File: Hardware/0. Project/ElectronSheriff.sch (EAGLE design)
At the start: 20 parts, among them Q2 AO3400, Q3 AO3400, U1 LM358D, U2 MAX4239AUTT

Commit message: Working on 1.0 schematic
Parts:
- U2: value MAX4239AUTT -> MAX4239
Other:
- moved on the sheet: C1
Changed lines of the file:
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@@
 <part name="R2" library="rcl" library_urn="urn:adsk.eagle:library:334" deviceset="R-EU_" device="R0603" package3d_urn="urn:adsk.eagle:package:23555/3" value="100k (1%)"/>
 <part name="BT1" library="1053" deviceset="1053" device="" value="CR2450"/>
-<part name="U2" library="MAX4239AUT+" deviceset="MAX4239AUTT" device=""/>
+<part name="U2" library="MAX4239AUT+" deviceset="MAX4239AUTT" device="" value="MAX4239"/>
 <part name="GND1" library="supply1" library_urn="urn:adsk.eagle:library:371" deviceset="0V" device=""/>
 <part name="PE1" library="supply1" library_urn="urn:adsk.eagle:library:371" deviceset="PE" device="" value=""/>
@@
 <attribute name="VALUE" x="242.57" y="73.66" size="1.778" layer="96" rot="R90"/>
 </instance>
-<instance part="C1" gate="G$1" x="254" y="113.03" smashed="yes">
-<attribute name="NAME" x="255.524" y="113.411" size="1.778" layer="95"/>
-<attribute name="VALUE" x="255.524" y="108.331" size="1.778" layer="96"/>
+<instance part="C1" gate="G$1" x="234.95" y="113.03" smashed="yes">
+<attribute name="NAME" x="236.474" y="113.411" size="1.778" layer="95"/>
+<attribute name="VALUE" x="236.474" y="108.331" size="1.778" layer="96"/>
 </instance>
 <instance part="R7" gate="G$1" x="199.39" y="130.81" smashed="yes">
@@
 <attribute name="VALUE" x="128.27" y="118.618" size="1.6764" layer="96"/>
 </instance>
-<instance part="PE5" gate="M" x="125.73" y="90.17" smashed="yes">
-<attribute name="VALUE" x="123.19" y="87.63" size="1.778" layer="96" rot="R90"/>
+<instance part="PE5" gate="M" x="125.73" y="76.2" smashed="yes">
+<attribute name="VALUE" x="123.19" y="73.66" size="1.778" layer="96" rot="R90"/>
 </instance>
 <instance part="R9" gate="G$1" x="153.67" y="120.65" smashed="yes" rot="R90">
@@
 <segment>
 <pinref part="PE5" gate="M" pin="PE"/>
-<wire x1="125.73" y1="92.71" x2="125.73" y2="95.25" width="0.1524" layer="91"/>
+<wire x1="125.73" y1="78.74" x2="125.73" y2="95.25" width="0.1524" layer="91"/>
 <pinref part="X1" gate="-2" pin="KL"/>
 <wire x1="113.03" y1="95.25" x2="125.73" y2="95.25" width="0.1524" layer="91"/>
@@
 <pinref part="U2" gate="A" pin="OUT"/>
 <pinref part="R4" gate="G$1" pin="2"/>
-<wire x1="227.33" y1="128.27" x2="245.11" y2="128.27" width="0.1524" layer="91"/>
+<wire x1="227.33" y1="128.27" x2="234.95" y2="128.27" width="0.1524" layer="91"/>
+<wire x1="234.95" y1="128.27" x2="245.11" y2="128.27" width="0.1524" layer="91"/>
 <wire x1="245.11" y1="128.27" x2="245.11" y2="124.46" width="0.1524" layer="91"/>
 <pinref part="C1" gate="G$1" pin="1"/>
-<wire x1="254" y1="115.57" x2="254" y2="128.27" width="0.1524" layer="91"/>
-<wire x1="254" y1="128.27" x2="245.11" y2="128.27" width="0.1524" layer="91"/>
-<junction x="245.11" y="128.27"/>
+<wire x1="234.95" y1="115.57" x2="234.95" y2="128.27" width="0.1524" layer="91"/>
+<junction x="234.95" y="128.27"/>
 </segment>
 </net>
@@
 <wire x1="209.55" y1="125.73" x2="207.01" y2="125.73" width="0.1524" layer="91"/>
 <wire x1="207.01" y1="125.73" x2="207.01" y2="95.25" width="0.1524" layer="91"/>
-<wire x1="207.01" y1="95.25" x2="245.11" y2="95.25" width="0.1524" layer="91"/>
+<wire x1="207.01" y1="95.25" x2="234.95" y2="95.25" width="0.1524" layer="91"/>
 <pinref part="R5" gate="G$1" pin="1"/>
+<wire x1="234.95" y1="95.25" x2="245.11" y2="95.25" width="0.1524" layer="91"/>
 <wire x1="245.11" y1="95.25" x2="245.11" y2="99.06" width="0.1524" layer="91"/>
 <pinref part="R6" gate="G$1" pin="2"/>
@@
 <junction x="245.11" y="95.25"/>
 <pinref part="C1" gate="G$1" pin="2"/>
-<wire x1="254" y1="107.95" x2="254" y2="95.25" width="0.1524" layer="91"/>
-<wire x1="254" y1="95.25" x2="245.11" y2="95.25" width="0.1524" layer="91"/>
-</segment>
-</net>
+<wire x1="234.95" y1="107.95" x2="234.95" y2="95.25" width="0.1524" layer="91"/>
+<junction x="234.95" y="95.25"/>
+</segment>
+</net>

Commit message: Working on 1.0 schematic
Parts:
- added C10, C13: 15 pF, rcl:C-EUC0603
- added C11, C5: DNP, rcl:C-EUC0603
- added C12, C9: 6 pF, rcl:C-EUC0603
- added C14: 0.8 pF, rcl:C-EUC0603
- added C18, C19, C7, C8: 100 nF, rcl:C-EUC0603
- added C20, C22: 1uF, rcl:C-EUC0603
- added C21: 4.7 uF, rcl:C-EUC0603
- added C6: 100 pF, rcl:C-EUC0603
- added E1: ANT, SparkFun-RF:ANTENNA-GROUNDEDTRACE-15.2MM
- added J1: (no value), SparkFun-Connectors:ARDUINO_SERIAL_PROGRAMPTH
- added J5: CORTEX_DEBUGPTH, SparkFun-Connectors:CORTEX_DEBUGPTH
- added JP1: VDD-EN, SparkFun-Jumpers:JUMPER-SMT_2_NC_TRACE_SILK
- added L1: 3.9nH, nrf52832-breakout-temp:INDUCTOR-0402-3.9NH
- added SW1: TACTILE_SWITCH_SMD_4_6X2_8MM, SparkFun-Electromechanical:SWITCH_SPST_4_PINRECT
- added TP1, TP2: TEST-POINT3X4, SparkFun-Connectors:TEST-POINT3X4
- added U3: NRF52832, nrf52832-breakout-temp:NRF52832
- added U5: LM321MF, linear:LM321MF
- added Y1: 32MHz, nrf52832-breakout-temp:CRYSTAL-32MHZ-SMD-2.0X1.6MM
- added Y2: 32.768kHz, SparkFun-Clocks:CRYSTAL-32.768KHZSMD-3.2X1.5
- U1: value LM358D -> XC6206; device linear:LM358D -> XC6206:PMIC-LDO-XC6206P332MR-G(SOT23)
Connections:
- new net BLE_ANT: C14.1, L1.2, U3.ANT
- new net CRYSTAL_XC1: C12.1, U3.XC1(32MHZ), Y1.2
- new net CRYSTAL_XC2: C9.1, U3.XC2(32MHZ), Y1.1
- new net CRYSTAL_XL1: C10.1, U3.P0.00/XL1, Y2.2
- new net CRYSTAL_XL2: C13.1, U3.P0.01/XL2, Y2.1
- new net GND: C20.2, C22.2, J1.GND, J5.GND@3, J5.GND@5, J5.GNDDTCT, SW1.3, SW1.4, U1.GND
- new net MCU_!RESET!: J5.!RESET, SW1.1, SW1.2, U3.P0.21/RESET
- new net N$11: C11.1, E1.SIGNAL, L1.1
- new net N$12: C5.1, U3.DEC2
- new net N$13: C6.1, U3.DEC3
- new net N$14: J1.VCC, JP1.1
- new net N$15: C7.1, U3.DEC4
- new net N$8: C18.1, U3.DEC1
- new net P02: U3.P0.02/AIN0
- new net P03: U3.P0.03/AIN1
- new net P04: U3.P0.04/AIN2
- new net P05: U3.P0.05/AIN3
- new net P06: U3.P0.06
- new net P07: U3.P0.07
- new net P08: U3.P0.08
- new net P11: U3.P0.11
- new net P12: U3.P0.12
- new net P13: U3.P0.13
- new net P14: U3.P0.14
- new net P15: U3.P0.15
- new net P16: U3.P0.16
- new net P17: U3.P0.17
- new net P18: J5.SWO/TDO, U3.P0.18
- new net P19: U3.P0.19
- new net P20: U3.P0.20
- new net P22: U3.P0.22
- new net P23: U3.P0.23
- new net P24: U3.P0.24
- new net P25: U3.P0.25
- new net P26: J1.TXO, U3.P0.26
- new net P27: J1.RXI, U3.P0.27
- new net P28: U3.P0.28/AIN4
- new net P29: U3.P0.29/AIN5
- new net P30: U3.P0.30/AIN6
- new net P31: U3.P0.31/AIN7
- new net SWDCLK: J5.SWDCLK/TCK, TP2.1, U3.SWDCLK
- new net SWDIO: J5.SWDIO/TMS, TP1.1, U3.SWDIO
- new net VDD: C19.1, C20.1, C21.1, C8.1, J5.VCC, JP1.2, U1.OUT, U3.VDD
- new net VIN: C22.1, U1.IN
- net +5V: now also U5.V+; no longer U1P.V+
- net 0V: now also C10.2, C11.2, C12.2, C13.2, C14.2, C18.2, C19.2, C21.2, C5.2, C6.2, C7.2, C8.2, C9.2, E1.GND, U3.VSS, U5.V-; no longer U1P.V-
- net N$2: now also U5.+IN; no longer U1A.+IN
- net N$4: now also U5.-IN, U5.OUT; no longer U1A.-IN, U1A.OUT
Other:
- note added: "Buttons"
- note added: "Cortex Debug Connector"
- note added: "Open JP1 to disable powering the nRF52832 via a 3.3V FTDI Basic"
- note added: "Pin 13"
- note added: "Pin 36"
- note added: "Pin 48"
- note added: "Serial Program/Debug"

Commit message: Working on 1.0 schematic
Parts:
- removed SW1: TACTILE_SWITCH_SMD_4_6X2_8MM, SparkFun-Electromechanical:SWITCH_SPST_4_PINRECT
- removed TP1, TP2: TEST-POINT3X4, SparkFun-Connectors:TEST-POINT3X4
- removed U1: XC6206, XC6206:PMIC-LDO-XC6206P332MR-G(SOT23)
- added C15: 100 nF, rcl:C-EUC0603
- added C16: 1uF, rcl:C-EUC0603
- added C17: 100nF, rcl:C-EUC0603
- added S1: DTSM-3, switch-tact:DTSM-3
- C20: value 1uF -> 100nF
- C22: value 1uF -> 10uF; device rcl:C-EUC0603 -> rcl:C-EUC0805
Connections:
- net N$1 renamed ADC_AMMETER
- net P18 renamed MCU_SWO/TDO
- removed net GND: C20.2, C22.2, J1.GND, J5.GND@3, J5.GND@5, J5.GNDDTCT, SW1.3, SW1.4, U1.GND
- removed net MCU_!RESET!: J5.!RESET, SW1.1, SW1.2, U3.P0.21/RESET
- removed net SWDCLK: J5.SWDCLK/TCK, TP2.1, U3.SWDCLK
- removed net SWDIO: J5.SWDIO/TMS, TP1.1, U3.SWDIO
- removed net VIN: C22.1, U1.IN
- new net !MCU_RESET!: J5.!RESET, S1.2, U3.P0.21/RESET
- new net MCU_SWDCLK/TCK: J5.SWDCLK/TCK, U3.SWDCLK
- new net MCU_SWDIO/TMS: J5.SWDIO/TMS, U3.SWDIO
- new net MCU_TDI: J5.NC/TDI
- net +5V: now also C15.1, C16.1, C17.1, C19.1, C21.1, C8.1, J5.VCC, U3.VDD
- net 0V: now also C15.2, C16.2, C17.2, C20.2, C22.2, J1.GND, J5.GND@3, J5.GND@5, J5.GNDDTCT, S1.1
- net N$2: now also C20.1, C22.1
- net VDD: no longer C19.1, C20.1, C21.1, C8.1, J5.VCC, U1.OUT, U3.VDD
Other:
- note added: "2.4 GHz Bluetooth Transceiver"
- note added: "Bootloader Program and Debug Interface"
- note added: "JTAG/SWD Program and Debug Interface"
- note added: "Load Current Sense and Signal Conditioning"
- note added: "MCU External Oscillators"
- note added: "MCU Reset"
- note added: "Power Supply"
- note added: "Virtual Ground Reference"
- note added: "nRF52 SoC (Cortex M4 + Bluetooth 5)"
- note removed: "Buttons"
- note removed: "Cortex Debug Connector"
- note removed: "Serial Program/Debug"
- moved on the sheet: BT1, C1, C10, C11, C12, C13, C14, C18, C19, C2, C20, C21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

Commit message: Working on 1.0 schematic
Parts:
- removed C4: 100nF, rcl:C-EUC0603
- added R11: 220R (5%), rcl:R-EU_R0603
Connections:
- net 0V: now also C3.2; no longer C4.1
- net ADC_AMMETER: now also R11.1, R11.2
- net PE: no longer C3.2, C4.2
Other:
- moved on the sheet: BT1, C1, C10, C11, C12, C13, C14, C15, C16, C17, C18, C19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

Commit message: Working on 1.0 schematic
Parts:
- removed JP1: VDD-EN, SparkFun-Jumpers:JUMPER-SMT_2_NC_TRACE_SILK
- added C23, C4: 100nF, rcl:C-EUC0603
- added CN1: MicroSD Card, Micro SD:MICROSD-PUSH-OUT
- added CN2: DISPLAY-OLED-128X64-I2C, diy-modules:DISPLAY-OLED-128X64-I2C
- added R12: 0R (5%), rcl:R-EU_R0603
- added R13, R14, R15, R16, R17: 10k (5%), rcl:R-EU_R0603
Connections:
- removed net N$14: J1.VCC, JP1.1
- removed net PE: Q2.S, Q3.S, R3.2, R6.1, R8.1, X1-2.KL
- removed net VDD: JP1.2
- new net !MICROSD_SPI_CS!: CN1.2
- new net ADC_AMMETER_VOUT: R11.2
- new net ADC_VGND: R12.2
- new net DISPLAY_I2C_SCL: CN2.SCL, R16.1
- new net DISPLAY_I2C_SDA: CN2.SDA, R17.1
- new net MICROSD_SPI_CARD_DETECT: CN1.9, R15.1
- new net MICROSD_SPI_CLK: CN1.5
- new net MICROSD_SPI_MISO: CN1.7, R14.1
- new net MICROSD_SPI_MOSI: CN1.3, R13.1
- new net RANGE_MA: Q3.G
- new net RANGE_UA: Q2.G
- new net VGND: Q2.S, Q3.S, R12.1, R3.2, R6.1, R8.1, X1-2.KL
- net +5V: now also C23.1, C4.1, CN1.4, CN2.VCC, R13.2, R14.2, R15.2, R16.2, R17.2
- net 0V: now also C23.2, C4.2, CN1.10, CN1.6, CN2.GND
- net ADC_AMMETER: no longer R11.2
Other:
- note added: "Micro SD Memory Card interface"
- note removed: "Open JP1 to disable powering the nRF52832 via a 3.3V FTDI Basic"
- moved on the sheet: BT1, C1, C10, C11, C12, C13, C14, C15, C16, C17, C18, C19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

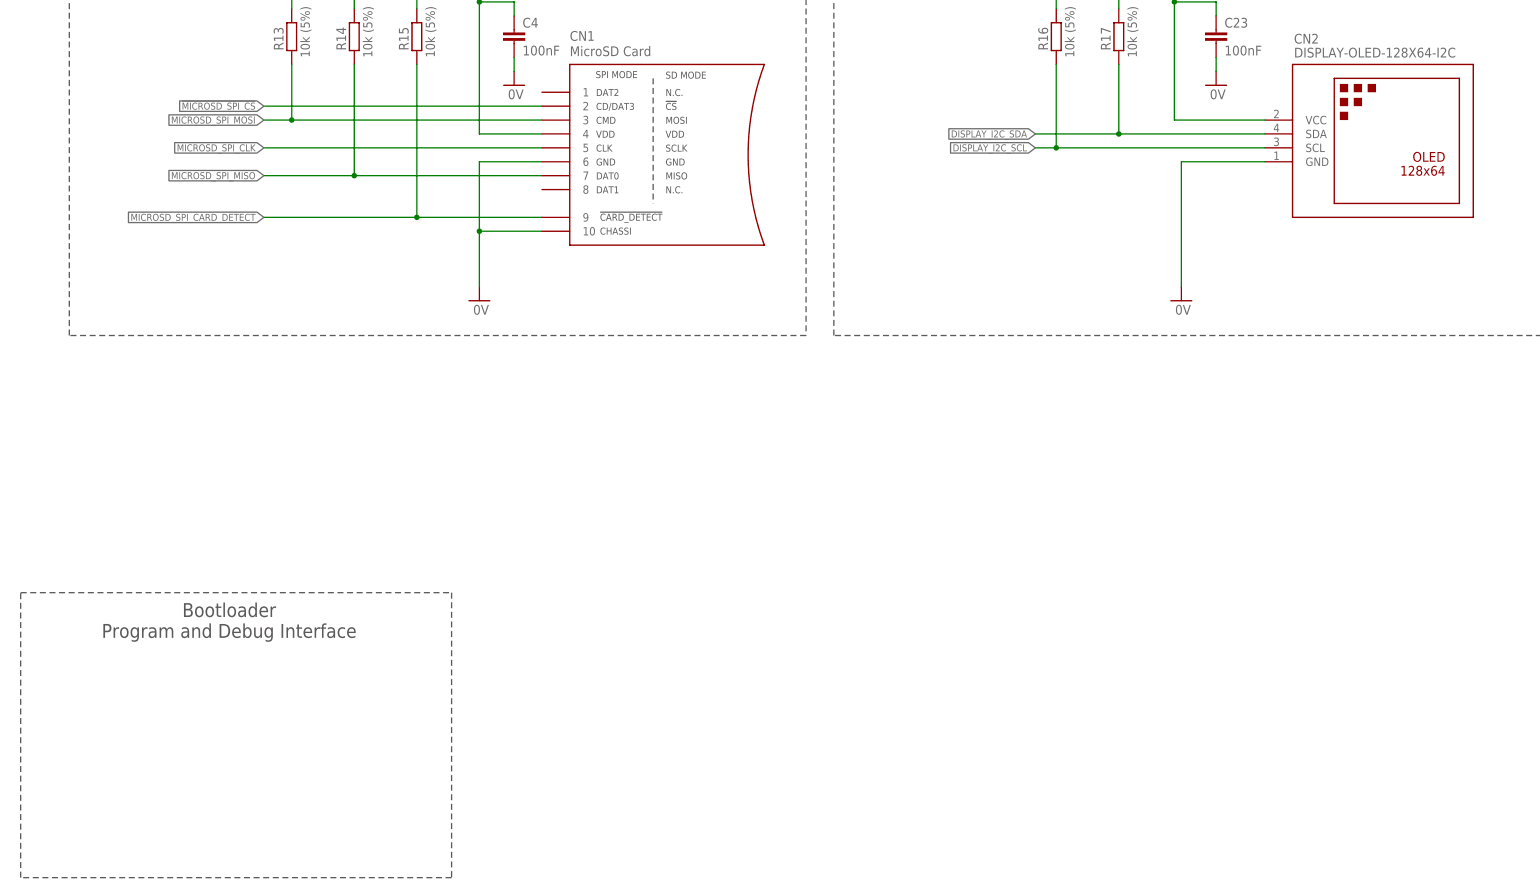
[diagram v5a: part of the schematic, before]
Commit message: OLED and SD-Card circuits added
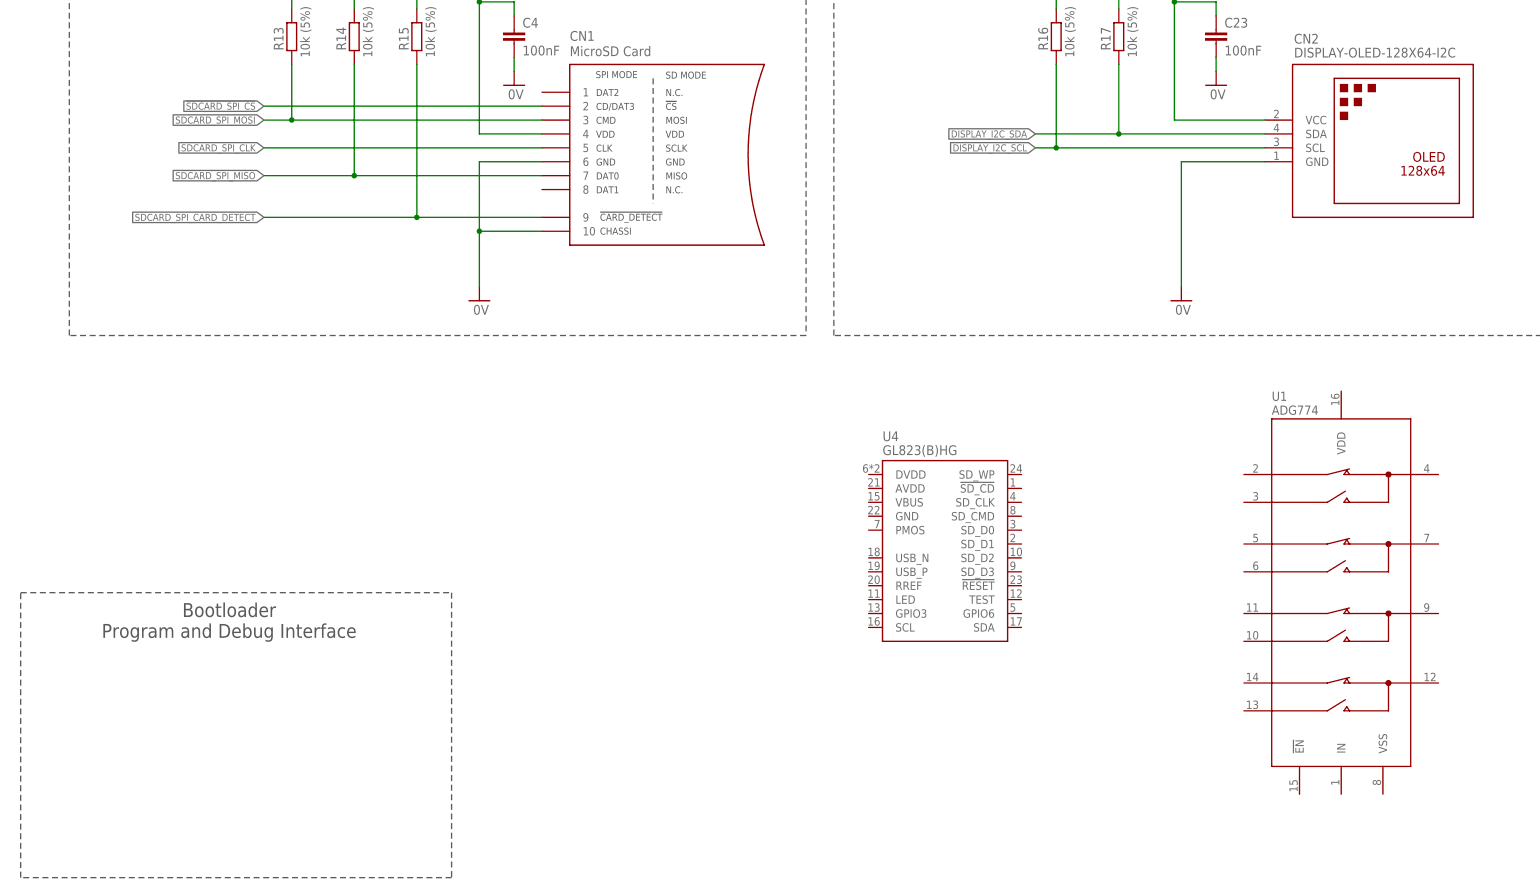
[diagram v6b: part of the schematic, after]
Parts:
- added U1: ADG774, ADG774:ADG774
- added U4: GL823(B)HG, GL823:GL823(B)HG
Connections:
- net !MICROSD_SPI_CS! renamed !SDCARD_SPI_CS!
- net MICROSD_SPI_CARD_DETECT renamed SDCARD_SPI_CARD_DETECT
- net MICROSD_SPI_CLK renamed SDCARD_SPI_CLK
- net MICROSD_SPI_MISO renamed SDCARD_SPI_MISO
- net MICROSD_SPI_MOSI renamed SDCARD_SPI_MOSI
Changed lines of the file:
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@@
 <setting verticaltext="up"/>
 </settings>
-<grid distance="0.05" unitdist="inch" unit="inch" style="lines" multiple="1" display="no" altdistance="0.01" altunitdist="inch" altunit="inch"/>
+<grid distance="0.1" unitdist="inch" unit="inch" style="lines" multiple="1" display="no" altdistance="0.01" altunitdist="inch" altunit="inch"/>
 <layers>
 <layer number="1" name="Top" color="4" fill="1" visible="no" active="no"/>
@@
 <part name="GND31" library="supply1" library_urn="urn:adsk.eagle:library:371" deviceset="0V" device=""/>
 <part name="GND32" library="supply1" library_urn="urn:adsk.eagle:library:371" deviceset="0V" device=""/>
+<part name="U4" library="GL823" deviceset="GL823(B)" device="HG"/>
+<part name="U1" library="ADG774" deviceset="ADG774" device=""/>
 </parts>
 <sheets>
@@
 <attribute name="VALUE" x="627.507" y="161.29" size="1.778" layer="96"/>
 </instance>
+<instance part="U4" gate="G$1" x="584.2" y="119.38" smashed="yes">
+<attribute name="NAME" x="574.04" y="138.176" size="1.778" layer="95"/>
+<attribute name="VALUE" x="574.04" y="135.636" size="1.778" layer="96"/>
+</instance>
+<instance part="U1" gate="G$1" x="655.32" y="109.22" smashed="yes">
+<attribute name="NAME" x="645.16" y="145.542" size="1.6764" layer="95"/>
+<attribute name="VALUE" x="645.16" y="143.002" size="1.6764" layer="95"/>
+</instance>
 </instances>
 <busses>
@@
 </segment>
 </net>
-<net name="!MICROSD_SPI_CS!" class="0">
+<net name="!SDCARD_SPI_CS!" class="0">
 <segment>
 <pinref part="CN1" gate="G$1" pin="2"/>
@@
 </segment>
 </net>
-<net name="MICROSD_SPI_MOSI" class="0">
+<net name="SDCARD_SPI_MOSI" class="0">
 <segment>
 <pinref part="CN1" gate="G$1" pin="3"/>
@@
 </segment>
 </net>
-<net name="MICROSD_SPI_CLK" class="0">
+<net name="SDCARD_SPI_CLK" class="0">
 <segment>
 <pinref part="CN1" gate="G$1" pin="5"/>
@@
 </segment>
 </net>
-<net name="MICROSD_SPI_MISO" class="0">
+<net name="SDCARD_SPI_MISO" class="0">
 <segment>
 <pinref part="CN1" gate="G$1" pin="7"/>
@@
 </segment>
 </net>
-<net name="MICROSD_SPI_CARD_DETECT" class="0">
+<net name="SDCARD_SPI_CARD_DETECT" class="0">
 <segment>
 <pinref part="CN1" gate="G$1" pin="9"/>

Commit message: SD-Card to USB Circuit Interface Added
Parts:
- added C24, C25, C27, C28, C29: 100nF, rcl:C-EUC0603
- added C26: 10uF, rcl:C-EUC0603
- added L3: BLM15HB221SN1, inductors:BLM15HB221SN1
- added LED1: (no value), led:LEDCHIPLED_0603
- added Q1: BC817, transistor-npn:BC817-16LT1SMD
- added R18, R20, R21: 10k (5%), rcl:R-EU_R0603
- added R19: 4K7 (5%), rcl:R-EU_R0603
- added R22: 680R (5%), rcl:R-EU_R0603
- added R23: 1k (5%), rcl:R-EU_R0603
- added U6: ADG774, ADG774:ADG774
- added X2: (no value), con-berg:PN87520
- U4: value GL823(B)HG -> GL823
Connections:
- removed net !SDCARD_SPI_CS!: CN1.2
- removed net SDCARD_SPI_CARD_DETECT: CN1.9, R15.1
- removed net SDCARD_SPI_CLK: CN1.5
- removed net SDCARD_SPI_MISO: CN1.7, R14.1
- removed net SDCARD_SPI_MOSI: CN1.3, R13.1
- new net !MCU_SPI_CS!: U1.S4B
- new net MCU_SPI_CLK: U6.S2B
- new net MCU_SPI_MISO: U1.S1B
- new net MCU_SPI_MOSI: U6.S1B
- new net MUX_SWITCH: Q1.C, R18.1, R21.1, U1.IN, U6.IN
- new net N$1: C26.2, C27.2, L3.1, U4.DVDD
- new net N$14: Q1.B, R19.1
- new net N$16: C28.2, U4.PMOS
- new net N$17: C29.2, U4.!RESET
- new net N$18: R22.1, U4.RREF
- new net N$19: L3.2, U4.AVDD
- new net N$21: U4.USB_N, X2.2
- new net N$22: U4.USB_P, X2.3
- new net N$23: R23.1, U4.LED
- new net N$24: LED1.A, R23.2
- new net SDCARD_CARD_DETECT: CN1.9, R15.1, U4.!SD_CD
- new net SDCARD_CLK: CN1.5, U6.D2
- new net SDCARD_CMD/MOSI: CN1.3, R13.1, U6.D1
- new net SDCARD_DAT0/MISO: CN1.7, R14.1, U1.D1
- new net SDCARD_DAT1: CN1.8, U1.D2
- new net SDCARD_DAT2: CN1.1, U1.D3
- new net SDCARD_DAT3/!CS!: CN1.2, U1.D4
- new net USB_CLK: U4.SD_CLK, U6.S2A
- new net USB_CMD: U4.SD_CMD, U6.S1A
- new net USB_DAT0: U1.S1A, U4.SD_D0
- new net USB_DAT1: U1.S2A, U4.SD_D1
- new net USB_DAT2: U1.S3A, U4.SD_D2
- new net USB_DAT3: U1.S4A, U4.SD_D3
- new net USB_VDD: R19.2, R20.1, U4.VBUS, X2.1
- net +5V: now also C24.1, C25.1, R18.2, R21.2, U1.VDD, U6.VDD
- net 0V: now also C24.2, C25.2, C26.1, C27.1, C28.1, C29.1, LED1.C, Q1.E, R20.2, R22.2, U1.!EN!, U1.VSS, U4.GND, U4.GPIO3, U4.GPIO6, U4.SCL, U4.SDA, U4.SD_WP, U4.TEST, U6.!EN!, U6.VSS, X2.4
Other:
- note added: "Micro SD-Card to USB Interface"
- moved on the sheet: CN1, CN2, R16, R17, U4

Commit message: Working on 1.0 schematic
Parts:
- removed R11: 220R (5%), rcl:R-EU_R0603
- added C30, C31, C32: 100nF, rcl:C-EUC0603
- added R24: 68k (0.05%), rcl:R-EU_R0603
- added R25: 10k (0.05%), rcl:R-EU_R0603
- added R26: 220R (5%), rcl:R-EU_R0603
- added U7: MAX4239, MAX4239AUT+:MAX4239AUTT
- C2: value 100nF -> 10pF
- R21: value 10k (5%) -> 22k (0.05%)
- R4: value 75k (0.05%) -> 22k (0.05%)
- R5: value 24k (0.05%) -> 68k (0.05%)
- R6: value 1k (0.05%) -> 10k (0.05%)
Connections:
- removed net MUX_SWITCH: Q1.C, R18.1, R21.1, U1.IN, U6.IN
- new net ADC_AMMETER1: C2.1, R21.2, R26.1, U7.OUT
- new net MUX_MCU2USB: Q1.C, R18.1, U1.IN, U6.IN
- new net N$20: R21.1, R24.2
- new net N$25: C2.2, R24.1, R25.2, U7.IN-
- net +5V: now also C30.1, C31.1, U7.!SHDN, U7.VCC; no longer C2.1, R21.2
- net 0V: now also C30.2, C31.2, C32.1, U7.GND; no longer C2.2
- net ADC_AMMETER: now also U7.IN+; no longer R11.1
- net ADC_AMMETER_VOUT: now also R26.2; no longer R11.2
- net USB_VDD: now also C32.2
- net VGND: now also R25.1
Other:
- note added: "MCU or USB Micro SD-Card Communication (MCU as default)"
- moved on the sheet: BT1, C1, C16, C17, C2, C23, C24, C25, C26, C27, C28, C29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
